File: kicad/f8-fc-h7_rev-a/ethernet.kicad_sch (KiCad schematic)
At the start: 37 parts, among them U1 DP83848TSQ/NOPB, Y3 50 MHz

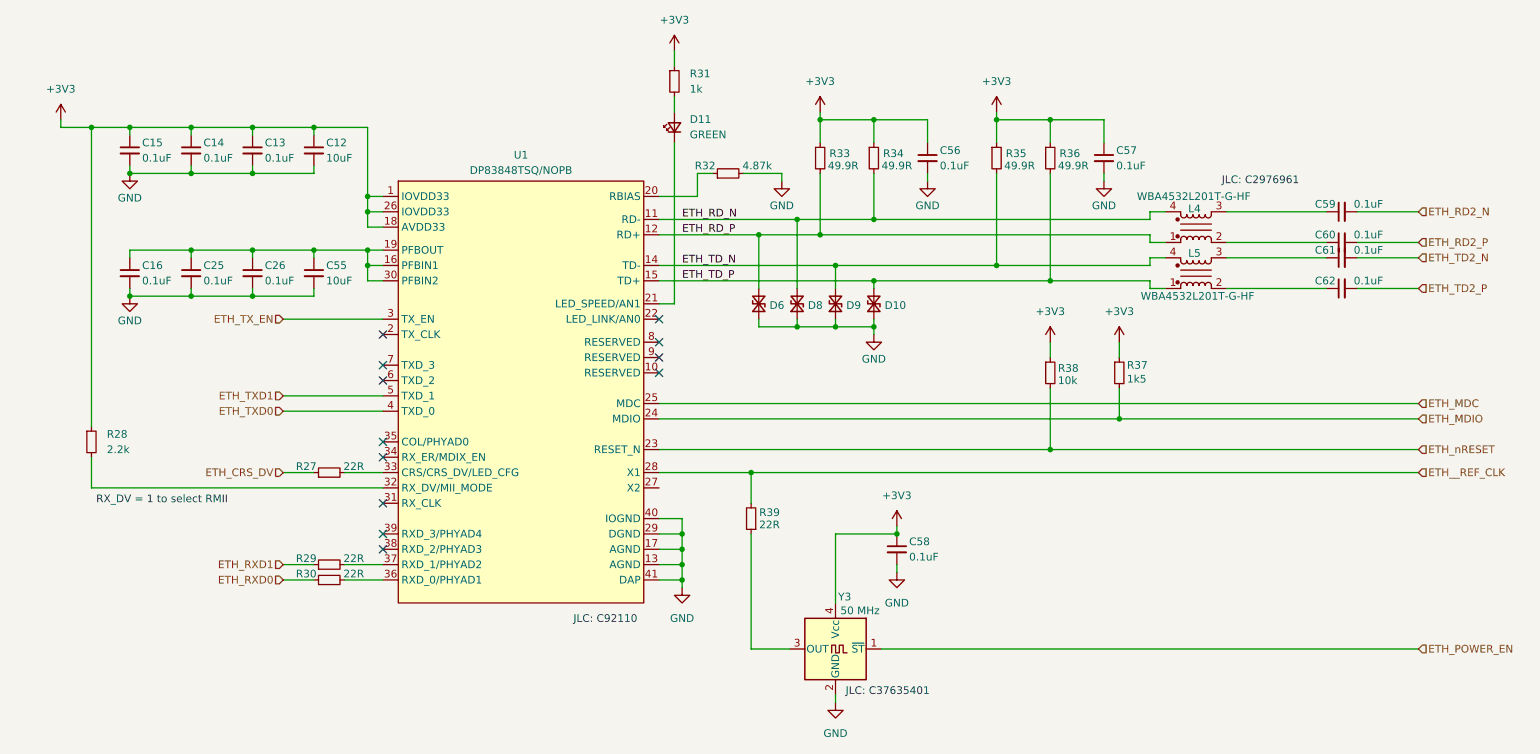
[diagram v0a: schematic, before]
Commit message: Swapped to LAN8742 Ethernet PHY
This was is supported by AP so seems more safe
to use this.
Also seems a bit simpler in wiring as it has a few less pins.
A downside is that I cannot find a proper application
schematic example online..
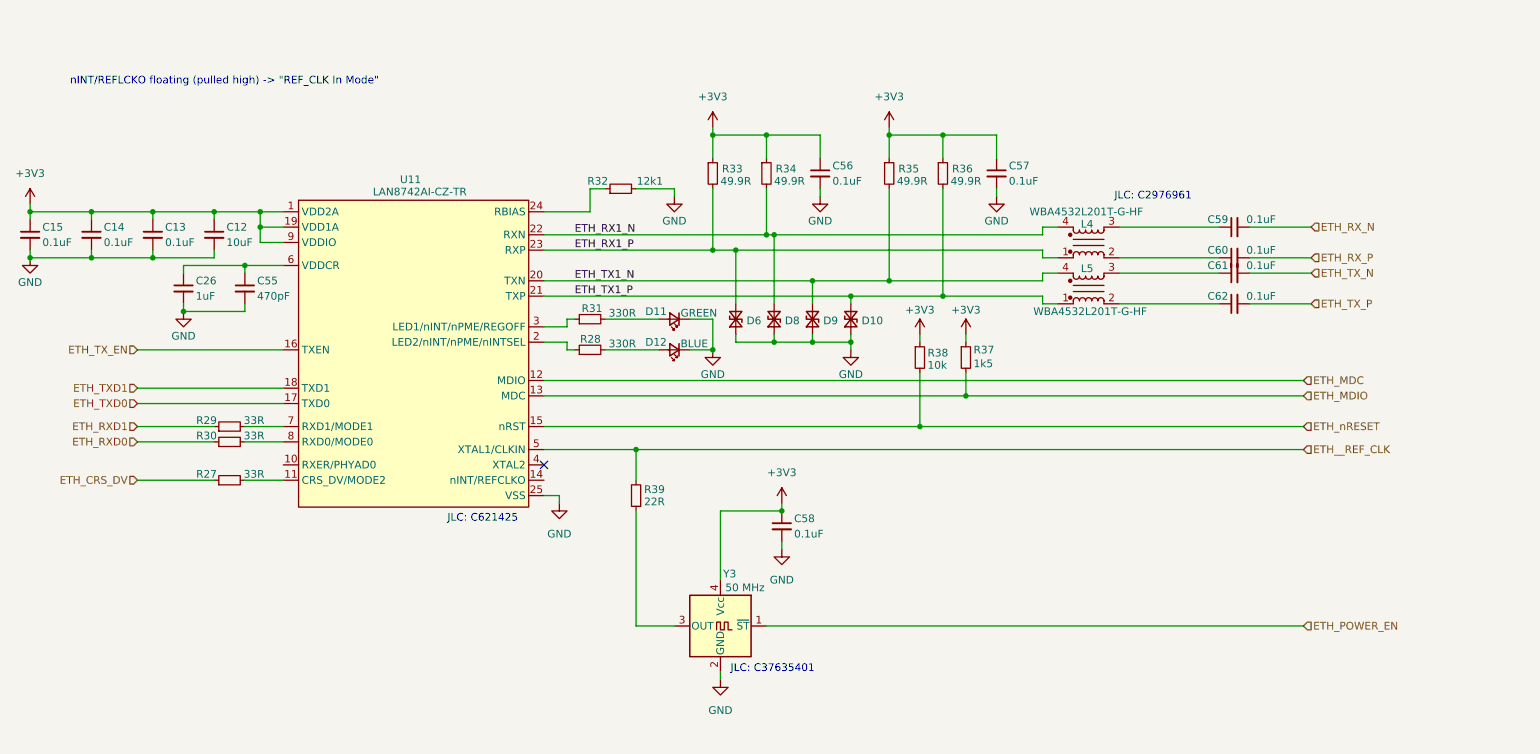
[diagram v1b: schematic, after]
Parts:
- removed C16, C25: 0.1uF, custom:C_0402_1005Metric_NoSilk, symbol Device:C_Small
- removed U1: DP83848TSQ/NOPB, easyeda2kicad:WQFN-40_L6.0-W6.0-P0.50-BL-EP, symbol easyeda2kicad:DP83848TSQ_NOPB
- added D12: BLUE, custom:LED_0603_1608Metric_NoSilk, symbol Device:LED_Small
- added U11: LAN8742AI-CZ-TR, easyeda2kicad:VQFN-24_L4.0-W4.0-P0.50-BL-EP2.5, symbol easyeda2kicad:LAN8742AI-CZ-TR
- C26: value 0.1uF -> 1uF
- C55: value 10uF -> 470pF
- R27, R29, R30: value 22R -> 33R
- R28: value 2.2k -> 330R
- R31: value 1k -> 330R
- R32: value 4.87k -> 12k1
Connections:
- net +3V3: now also U11.1 (VDD2A), U11.19 (VDD1A), U11.9 (VDDIO); no longer R28.1, R31.1
- net ETH_MDC: now also U11.12 (MDIO)
- net ETH_MDIO: now also U11.13 (MDC)
- net ETH_TXD0: now also U11.17 (TXD0)
- net ETH_TXD1: now also U11.18 (TXD1)
- net ETH_TX_EN: now also U11.16 (TXEN)
- net ETH__REF_CLK: now also U11.5 (XTAL1/CLKIN)
- net ETH_nRESET: now also U11.15 (nRST)
- net GND: now also D11.1 (K), D12.1 (K), U11.25 (VSS)
- net at C26.1, C55.1: now also U11.6 (VDDCR)
- net at R32.1: now also U11.24 (RBIAS)
- net at R28.2: now also D12.2 (A)
- net at R27.2: now also U11.11 (CRS_DV/MODE2)
- net at R30.2: now also U11.8 (RXD0/MODE0)
- net at R29.2: now also U11.7 (RXD1/MODE1)
- net ETH_RD2_N renamed ETH_RX_N
- net ETH_RD2_P renamed ETH_RX_P
- net ETH_RD_N renamed ETH_RX1_N
- net ETH_RX1_N: now also U11.22 (RXN)
- net ETH_RD_P renamed ETH_RX1_P
- net ETH_RX1_P: now also U11.23 (RXP)
- net ETH_TD2_N renamed ETH_TX_N
- net ETH_TD2_P renamed ETH_TX_P
- net ETH_TD_N renamed ETH_TX1_N
- net ETH_TX1_N: now also U11.20 (TXN)
- net ETH_TD_P renamed ETH_TX1_P
- net ETH_TX1_P: now also U11.21 (TXP)
- new net: R28.1, U11.2 (LED2/nINT/nPME/nINTSEL)
- new net: R31.1, U11.3 (LED1/nINT/nPME/REGOFF)
- no-connect marks 12 -> 1
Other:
- note added: "JLC: C621425"
- note added: "nINT/REFLCKO floating (pulled high) -> "REF_CLK In Mode""
- note removed: "JLC: C92110"
- note removed: "RX_DV = 1 to select RMII"
- moved on the sheet: C12, C13, C14, C15, C26, C55, C56, C57, C58, C59, C60, C61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
